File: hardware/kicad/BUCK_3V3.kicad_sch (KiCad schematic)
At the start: 0 parts

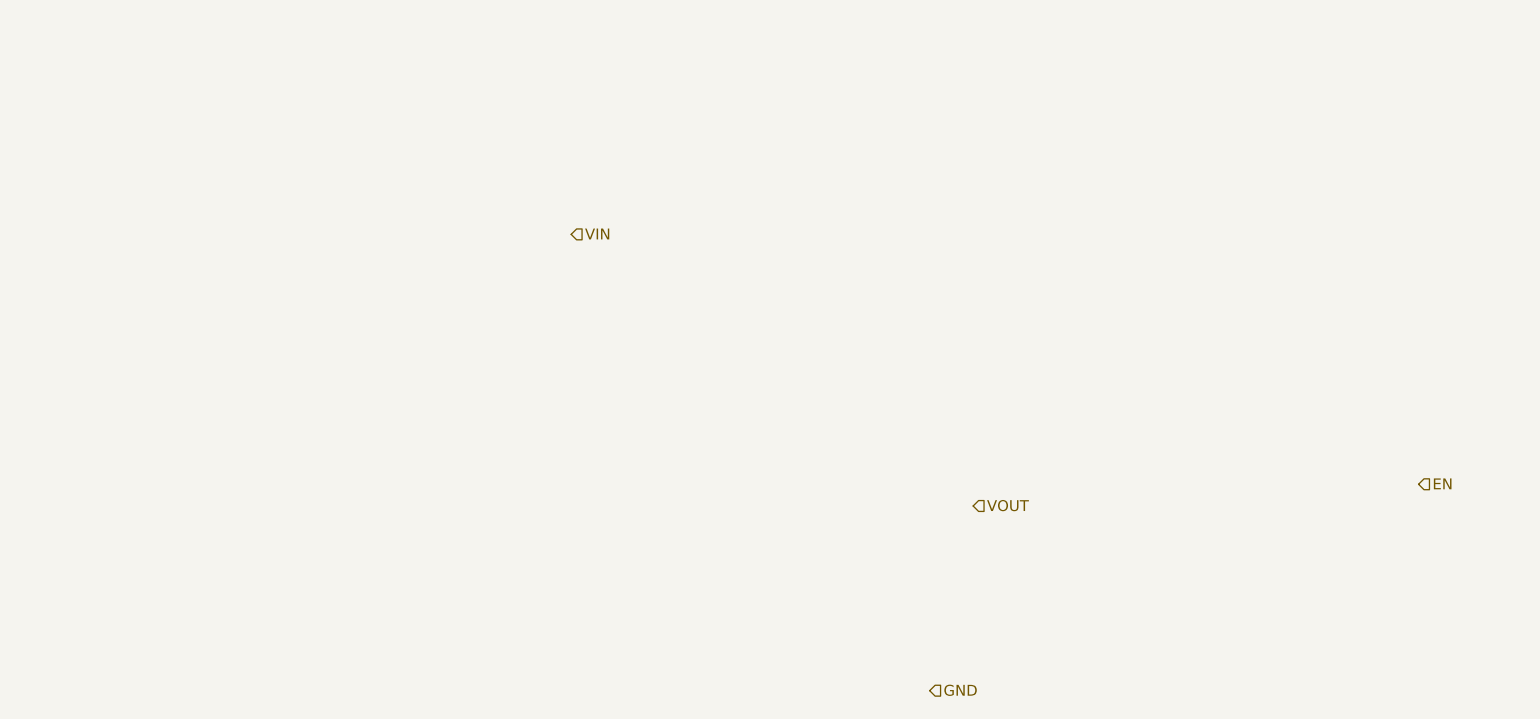
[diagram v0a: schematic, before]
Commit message: feat: added buck 12-5 & 12-3V3 layouts
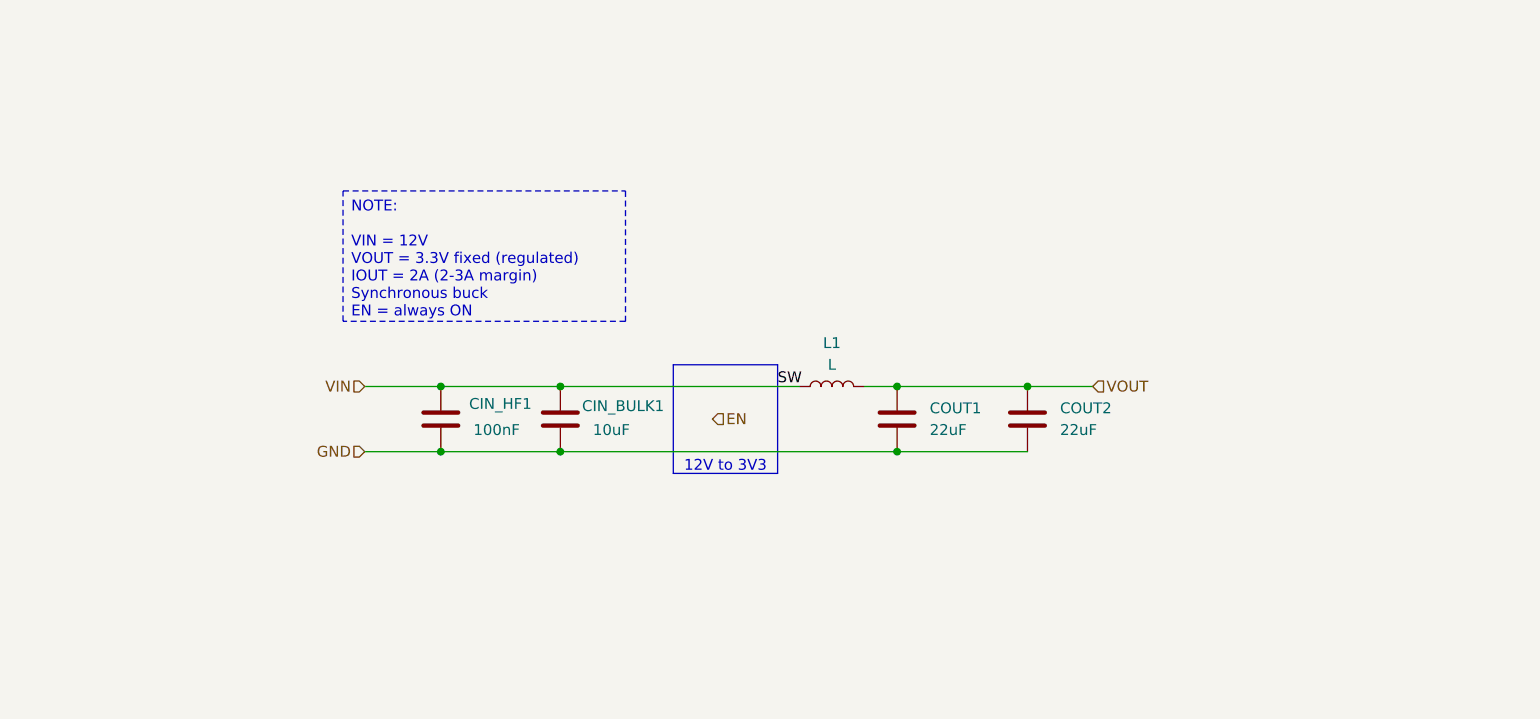
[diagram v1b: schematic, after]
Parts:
- added CIN_BULK1: 10uF, symbol Device:C
- added CIN_HF1: 100nF, symbol Device:C
- added COUT1, COUT2: 22uF, symbol Device:C
- added L1: L, symbol Device:L
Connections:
- net GND: now also CIN_BULK1.2, CIN_HF1.2, COUT1.2, COUT2.2
- net VIN: now also CIN_BULK1.1, CIN_HF1.1, L1.1
- net VOUT: now also COUT1.1, COUT2.1, L1.2
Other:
- note added: "12V to 3V3"

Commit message: feat: buck 12-3.3V schematic structure complete
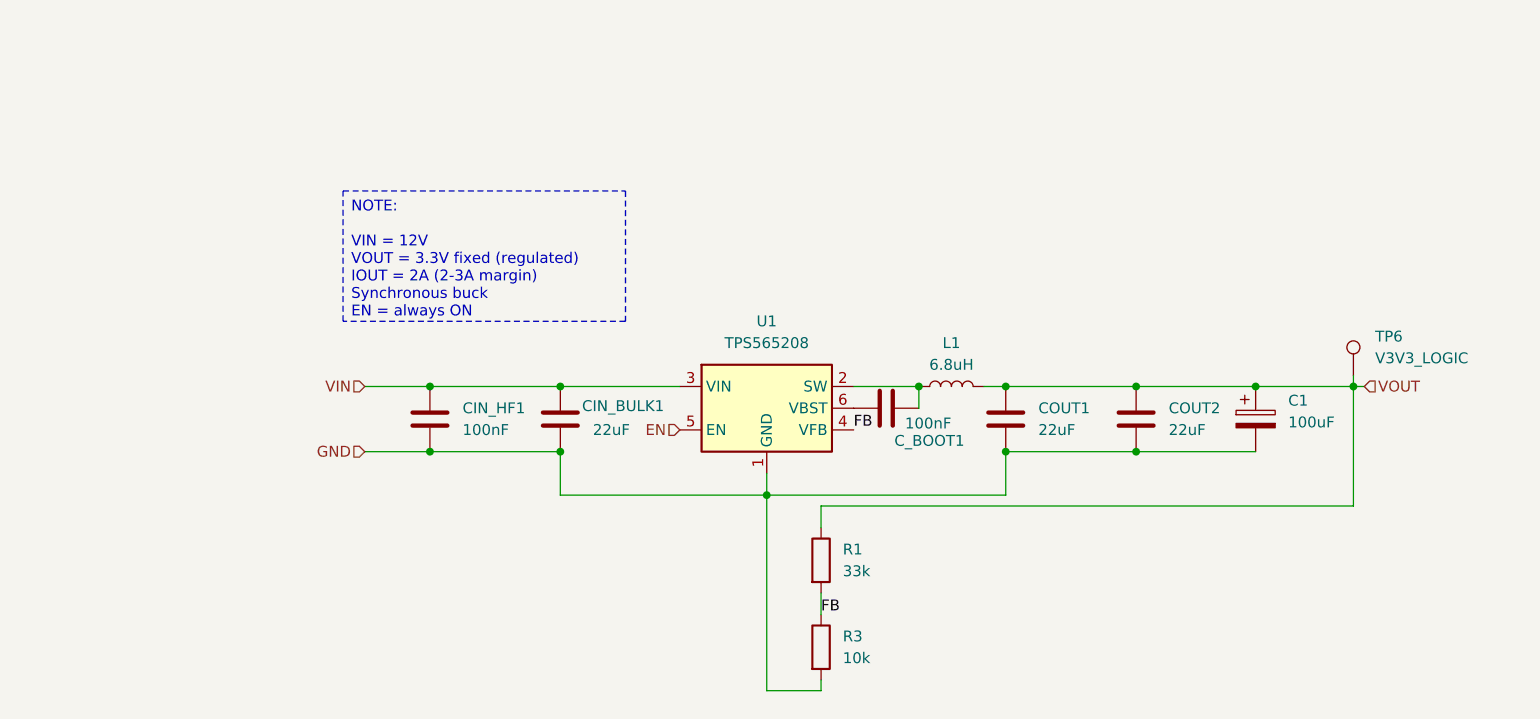
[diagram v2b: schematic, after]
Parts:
- added C1: 100uF, symbol Device:C_Polarized
- added C_BOOT1: 100nF, Capacitor_SMD:C_1210_3225Metric_Pad1.33x2.70mm_HandSolder, symbol Device:C
- added R1: 33k, Resistor_SMD:R_1210_3225Metric_Pad1.30x2.65mm_HandSolder, symbol Device:R
- added R3: 10k, symbol Device:R
- added TP6: V3V3_LOGIC, symbol Connector:TestPoint
- added U1: TPS565208, Package_TO_SOT_SMD:SOT-23-6_Handsoldering, symbol Regulator_Switching:TPS565208
- CIN_BULK1: value 10uF -> 22uF; footprint (none) -> Capacitor_SMD:C_1210_3225Metric_Pad1.33x2.70mm_HandSolder; Dielectric (none) -> X7R; Voltage (none) -> 25V
- CIN_HF1: footprint (none) -> Capacitor_SMD:C_1210_3225Metric_Pad1.33x2.70mm_HandSolder; Dielectric (none) -> X7R; Voltage  (none) -> 50V
- COUT1, COUT2: footprint (none) -> Capacitor_SMD:C_1210_3225Metric_Pad1.33x2.70mm_HandSolder; Dielectric (none) -> X7R; Voltage (none) -> 10V
- L1: value L -> 6.8uH; Irms (none) -> 2A (min); Isat (none) -> 6A
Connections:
- net EN: now also U1.5 (EN)
- net GND: now also C1.2, R3.2, U1.1 (GND)
- net VIN: now also U1.3 (VIN); no longer L1.1
- net VOUT: now also C1.1, R1.1, TP6.1
- new net: C_BOOT1.2, L1.1, U1.2 (SW)
- new net: C_BOOT1.1, U1.6 (VBST)
- new net FB: R1.2, R3.1, U1.4 (VFB)
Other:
- note removed: "12V to 3V3"
- moved on the sheet: CIN_HF1, COUT1, COUT2, L1

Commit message: fix: changed to TPSM82903 - PG not connected yet
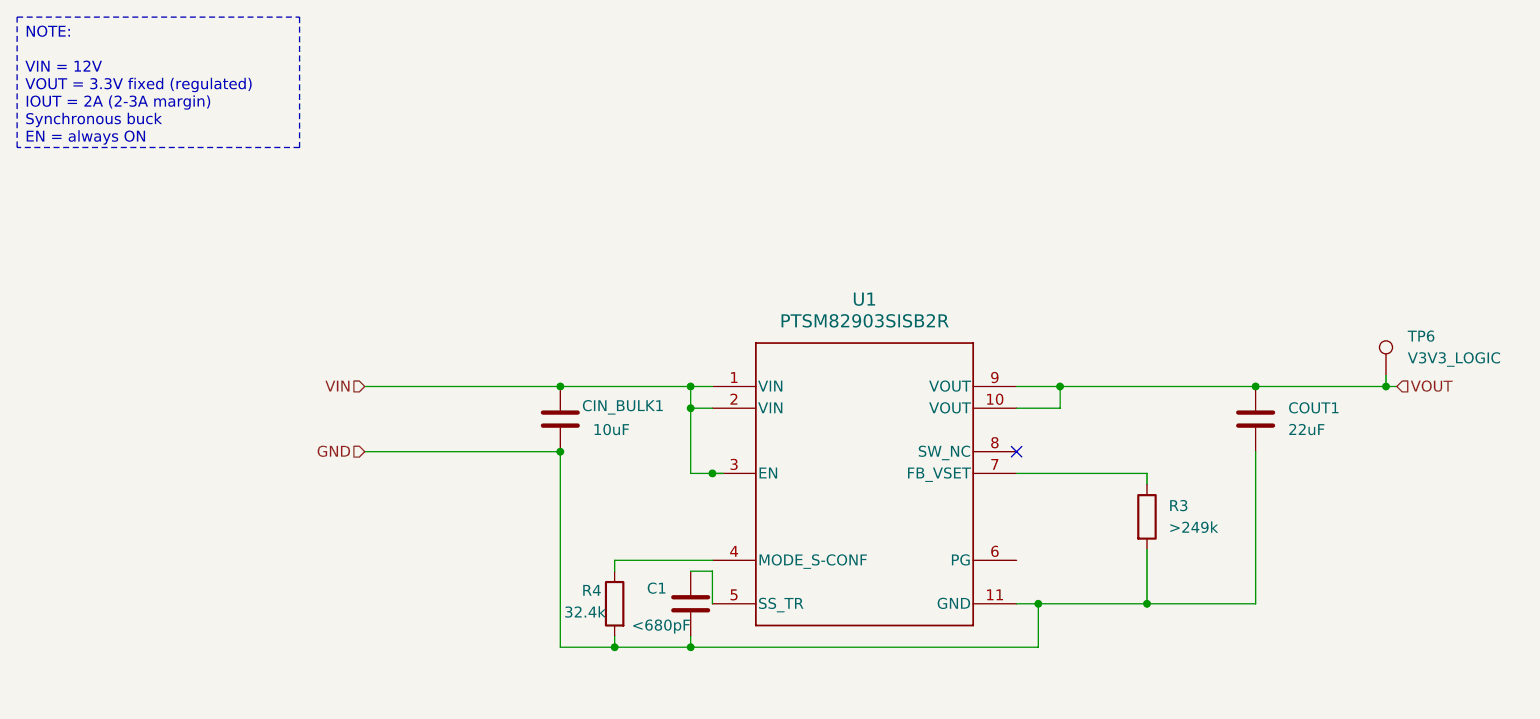
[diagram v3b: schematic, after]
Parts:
- removed C1: 100uF, symbol Device:C_Polarized
- removed CIN_HF1, C_BOOT1: 100nF, Capacitor_SMD:C_1210_3225Metric_Pad1.33x2.70mm_HandSolder, symbol Device:C
- removed COUT2: 22uF, Capacitor_SMD:C_1210_3225Metric_Pad1.33x2.70mm_HandSolder, symbol Device:C
- removed L1: 6.8uH, symbol Device:L
- removed R1: 33k, Resistor_SMD:R_1210_3225Metric_Pad1.30x2.65mm_HandSolder, symbol Device:R
- removed U1: TPS565208, Package_TO_SOT_SMD:SOT-23-6_Handsoldering, symbol Regulator_Switching:TPS565208
- added C1: <680pF, symbol Device:C
- added R4: 32.4k, symbol Device:R
- added U1: PTSM82903SISB2R, SIS0011A-MFG, symbol TPSM82903:PTSM82903SISB2R
- CIN_BULK1: value 22uF -> 10uF
- R3: value 10k -> >249k
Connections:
- net GND: now also C1.1, R4.2, U1.11 (GND)
- net VIN: now also U1.1 (VIN), U1.2 (VIN), U1.3 (EN)
- net VOUT: now also U1.10 (VOUT), U1.9 (VOUT)
- net FB: no longer names the net of R3.1
- net FB: now also U1.7 (FB_VSET)
- new net: C1.2, U1.5 (SS_TR)
- new net: R4.1, U1.4 (MODE_S-CONF)
- no-connect marks 0 -> 1
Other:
- moved on the sheet: COUT1, TP6

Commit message: fix: error fixing & connection config
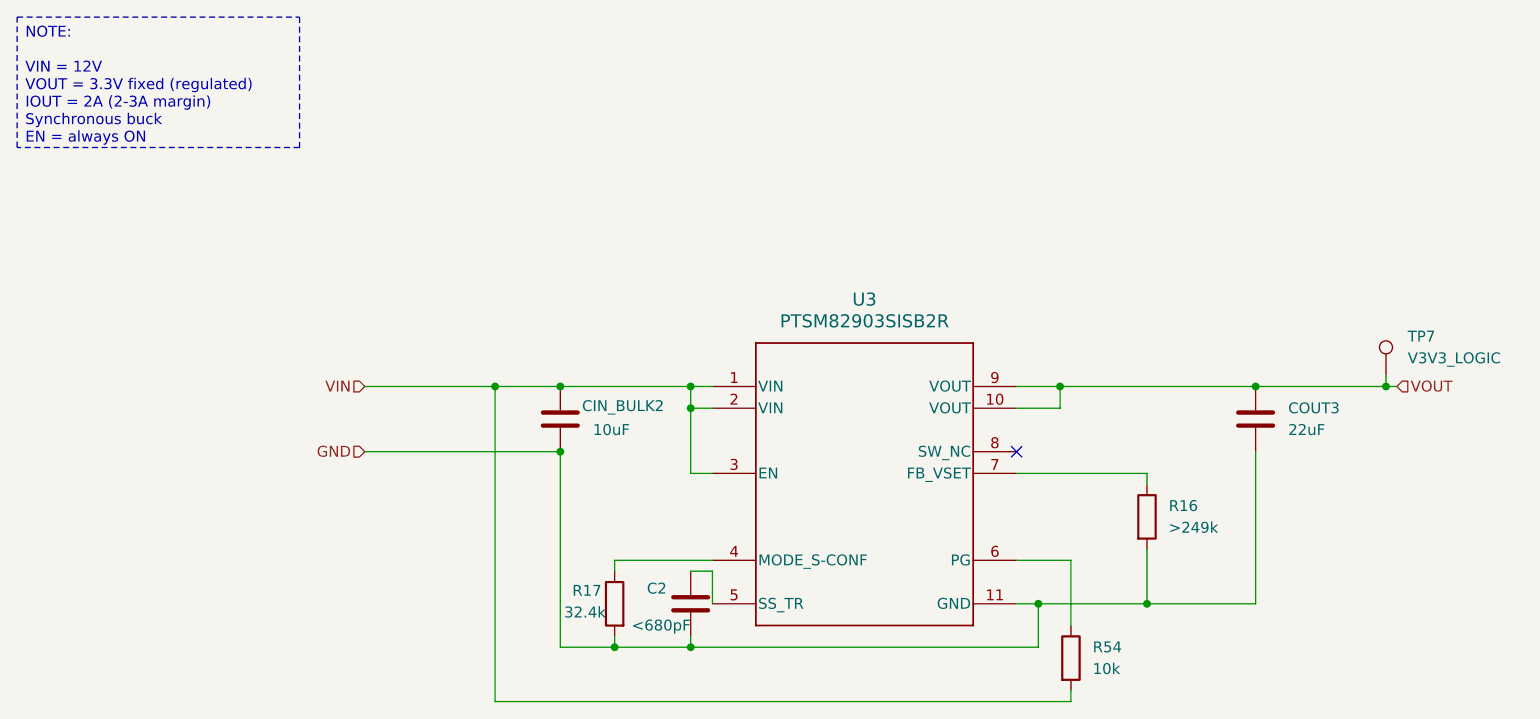
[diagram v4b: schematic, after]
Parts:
- added R54: 10k, symbol Device:R
- renumbered C1 to C2, CIN_BULK1 to CIN_BULK2, COUT1 to COUT3, R3 to R16, R4 to R17, TP6 to TP7, U1 to U3
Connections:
- net VIN: now also R54.2
- net at U3.6 (PG): now also R54.1
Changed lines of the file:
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@@
+	)
+	(junction
+		(at 102.87 90.17)
+		(diameter 0)
+		(color 0 0 0 0)
+	)
+	(junction
+		(at 80.01 90.17)
+		(diameter 0)
+		(color 0 0 0 0)
 	)
 	(junction
@@
 	)
 	(junction
-		(at 105.41 100.33)
-		(diameter 0)
-		(color 0 0 0 0)
-	)
-	(junction
 		(at 87.63 90.17)
 		(diameter 0)
@@
 	(junction
 		(at 156.21 115.57)
-		(diameter 0)
-		(color 0 0 0 0)
-	)
-	(junction
-		(at 102.87 90.17)
 		(diameter 0)
 		(color 0 0 0 0)
@@
 	(wire
 		(pts
+			(xy 80.01 90.17) (xy 80.01 127)
+		)
+		(stroke
+			(width 0)
+			(type default)
+		)
+	)
+	(wire
+		(pts
 			(xy 93.98 120.65) (xy 102.87 120.65)
 		)
@@
 	(wire
 		(pts
+			(xy 147.32 127) (xy 147.32 125.73)
+		)
+		(stroke
+			(width 0)
+			(type default)
+		)
+	)
+	(wire
+		(pts
 			(xy 105.41 100.33) (xy 102.87 100.33)
 		)
@@
 	(wire
 		(pts
+			(xy 80.01 127) (xy 147.32 127)
+		)
+		(stroke
+			(width 0)
+			(type default)
+		)
+	)
+	(wire
+		(pts
 			(xy 146.05 90.17) (xy 168.91 90.17)
 		)
@@
 	(wire
 		(pts
+			(xy 105.41 92.71) (xy 102.87 92.71)
+		)
+		(stroke
+			(width 0)
+			(type default)
+		)
+	)
+	(wire
+		(pts
+			(xy 64.77 90.17) (xy 80.01 90.17)
+		)
+		(stroke
+			(width 0)
+			(type default)
+		)
+	)
+	(wire
+		(pts
 			(xy 102.87 90.17) (xy 105.41 90.17)
 		)
@@
 	(wire
 		(pts
-			(xy 105.41 92.71) (xy 102.87 92.71)
-		)
-		(stroke
-			(width 0)
-			(type default)
-		)
-	)
-	(wire
-		(pts
-			(xy 64.77 90.17) (xy 87.63 90.17)
-		)
-		(stroke
-			(width 0)
-			(type default)
-		)
-	)
-	(wire
-		(pts
-			(xy 105.41 100.33) (xy 106.68 100.33)
-		)
-		(stroke
-			(width 0)
-			(type default)
-		)
-	)
-	(wire
-		(pts
 			(xy 102.87 119.38) (xy 102.87 120.65)
 		)
@@
 	(wire
 		(pts
+			(xy 140.97 110.49) (xy 147.32 110.49)
+		)
+		(stroke
+			(width 0)
+			(type default)
+		)
+	)
+	(wire
+		(pts
 			(xy 168.91 115.57) (xy 168.91 97.79)
 		)
@@
 	(wire
 		(pts
+			(xy 80.01 90.17) (xy 87.63 90.17)
+		)
+		(stroke
+			(width 0)
+			(type default)
+		)
+	)
+	(wire
+		(pts
 			(xy 102.87 100.33) (xy 102.87 92.71)
 		)
@@
 		(pts
 			(xy 156.21 100.33) (xy 156.21 101.6)
+		)
+		(stroke
+			(width 0)
+			(type default)
+		)
+	)
+	(wire
+		(pts
+			(xy 147.32 110.49) (xy 147.32 118.11)
 		)
 		(stroke
@@
 		(on_board yes)
 		(dnp no)
-		(property "Reference" "CIN_BULK1"
+		(property "Reference" "CIN_BULK2"
 			(at 90.17 92.456 0)
 			(effects
@@
 			(project ""
 				(path "/0357579f-0f06-4880-b651-8e2778a9baa9/2731e8ed-07c3-48e2-8ff5-054edae4aa44/900cc117-784e-40e9-8730-d957525d55d8"
-					(reference "CIN_BULK1")
+					(reference "CIN_BULK2")
 					(unit 1)
 				)
@@
 		(on_board yes)
 		(dnp no)
-		(property "Reference" "C1"
+		(property "Reference" "C2"
 			(at 100.076 113.792 0)
 			(effects
@@
 			(project ""
 				(path "/0357579f-0f06-4880-b651-8e2778a9baa9/2731e8ed-07c3-48e2-8ff5-054edae4aa44/900cc117-784e-40e9-8730-d957525d55d8"
-					(reference "C1")
+					(reference "C2")
 					(unit 1)
 				)
@@
 		(dnp no)
 		(fields_autoplaced yes)
-		(property "Reference" "COUT1"
+		(property "Reference" "COUT3"
 			(at 172.72 92.7099 0)
 			(effects
@@
 			(project ""
 				(path "/0357579f-0f06-4880-b651-8e2778a9baa9/2731e8ed-07c3-48e2-8ff5-054edae4aa44/900cc117-784e-40e9-8730-d957525d55d8"
-					(reference "COUT1")
+					(reference "COUT3")
 					(unit 1)
 				)
@@
 		(on_board yes)
 		(dnp no)
-		(property "Reference" "TP6"
+		(property "Reference" "TP7"
 			(at 186.69 84.3279 0)
 			(effects
@@
 			(project ""
 				(path "/0357579f-0f06-4880-b651-8e2778a9baa9/2731e8ed-07c3-48e2-8ff5-054edae4aa44/900cc117-784e-40e9-8730-d957525d55d8"
-					(reference "TP6")
+					(reference "TP7")
 					(unit 1)
 				)
@@
 		(on_board yes)
 		(dnp no)
-		(property "Reference" "R4"
+		(property "Reference" "R17"
 			(at 92.456 114.046 0)
 			(effects
@@
 			(project ""
 				(path "/0357579f-0f06-4880-b651-8e2778a9baa9/2731e8ed-07c3-48e2-8ff5-054edae4aa44/900cc117-784e-40e9-8730-d957525d55d8"
-					(reference "R4")
+					(reference "R17")
 					(unit 1)
 				)
@@
 		(dnp no)
 		(fields_autoplaced yes)
-		(property "Reference" "R3"
+		(property "Reference" "R16"
 			(at 158.75 104.1399 0)
 			(effects
@@
 			(project ""
 				(path "/0357579f-0f06-4880-b651-8e2778a9baa9/2731e8ed-07c3-48e2-8ff5-054edae4aa44/900cc117-784e-40e9-8730-d957525d55d8"
-					(reference "R3")
+					(reference "R16")
+					(unit 1)
+				)
+			)
+		)
+	)
+	(symbol
+		(lib_id "Device:R")
+		(at 147.32 121.92 0)
+		(unit 1)
+		(exclude_from_sim no)
+		(in_bom yes)
+		(on_board yes)
+		(dnp no)
+		(fields_autoplaced yes)
+		(property "Reference" "R54"
+			(at 149.86 120.6499 0)
+			(effects
+				(font
+					(size 1.27 1.27)
+				)
+				(justify left)
+			)
+		)
+		(property "Value" "10k"
+			(at 149.86 123.1899 0)
+			(effects
+				(font
+					(size 1.27 1.27)
+				)
+				(justify left)
+			)
+		)
+		(property "Footprint" ""
+			(at 145.542 121.92 90)
+			(effects
+				(font
+					(size 1.27 1.27)
+				)
+				(hide yes)
+			)
+		)
+		(property "Datasheet" "~"
+			(at 147.32 121.92 0)
+			(effects
+				(font
+					(size 1.27 1.27)
+				)
+				(hide yes)
+			)
+		)
+		(property "Description" "Resistor"
+			(at 147.32 121.92 0)
+			(effects
+				(font
+					(size 1.27 1.27)
+				)
+				(hide yes)
+			)
+		)
+		(pin "1"
+		)
+		(pin "2"
+		)
+		(instances
+			(project ""
+				(path "/0357579f-0f06-4880-b651-8e2778a9baa9/2731e8ed-07c3-48e2-8ff5-054edae4aa44/900cc117-784e-40e9-8730-d957525d55d8"
+					(reference "R54")
 					(unit 1)
 				)
@@
 		(dnp no)
 		(fields_autoplaced yes)
-		(property "Reference" "U1"
+		(property "Reference" "U3"
 			(at 123.19 80.01 0)
 			(effects
@@
 			(project ""
 				(path "/0357579f-0f06-4880-b651-8e2778a9baa9/2731e8ed-07c3-48e2-8ff5-054edae4aa44/900cc117-784e-40e9-8730-d957525d55d8"
-					(reference "U1")
+					(reference "U3")
 					(unit 1)
 				)

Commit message: docs: added end semester report for project
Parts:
- C2, CIN_BULK2, COUT3: symbol Device:C -> TPSM82903:C
- R16, R17, R54: symbol Device:R -> TPSM82903:R
- TP7: symbol Connector:TestPoint -> TPSM82903:TestPoint
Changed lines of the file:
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@@
 	)
 	(symbol
-		(lib_id "Device:C")
+		(lib_id "TPSM82903:C")
 		(at 87.63 93.98 0)
 		(unit 1)
@@
 	)
 	(symbol
-		(lib_id "Device:C")
+		(lib_id "TPSM82903:C")
 		(at 102.87 115.57 0)
 		(mirror x)
@@
 	)
 	(symbol
-		(lib_id "Device:C")
+		(lib_id "TPSM82903:C")
 		(at 168.91 93.98 0)
 		(unit 1)
@@
 	)
 	(symbol
-		(lib_id "Connector:TestPoint")
+		(lib_id "TPSM82903:TestPoint")
 		(at 184.15 88.9 0)
 		(unit 1)
@@
 	)
 	(symbol
-		(lib_id "Device:R")
+		(lib_id "TPSM82903:R")
 		(at 93.98 115.57 0)
 		(mirror y)
@@
 	)
 	(symbol
-		(lib_id "Device:R")
+		(lib_id "TPSM82903:R")
 		(at 156.21 105.41 0)
 		(unit 1)
@@
 	)
 	(symbol
-		(lib_id "Device:R")
+		(lib_id "TPSM82903:R")
 		(at 147.32 121.92 0)
 		(unit 1)
